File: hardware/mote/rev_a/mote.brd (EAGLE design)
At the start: 160 x 100 mm, 13 parts, among them U1 NRF52840

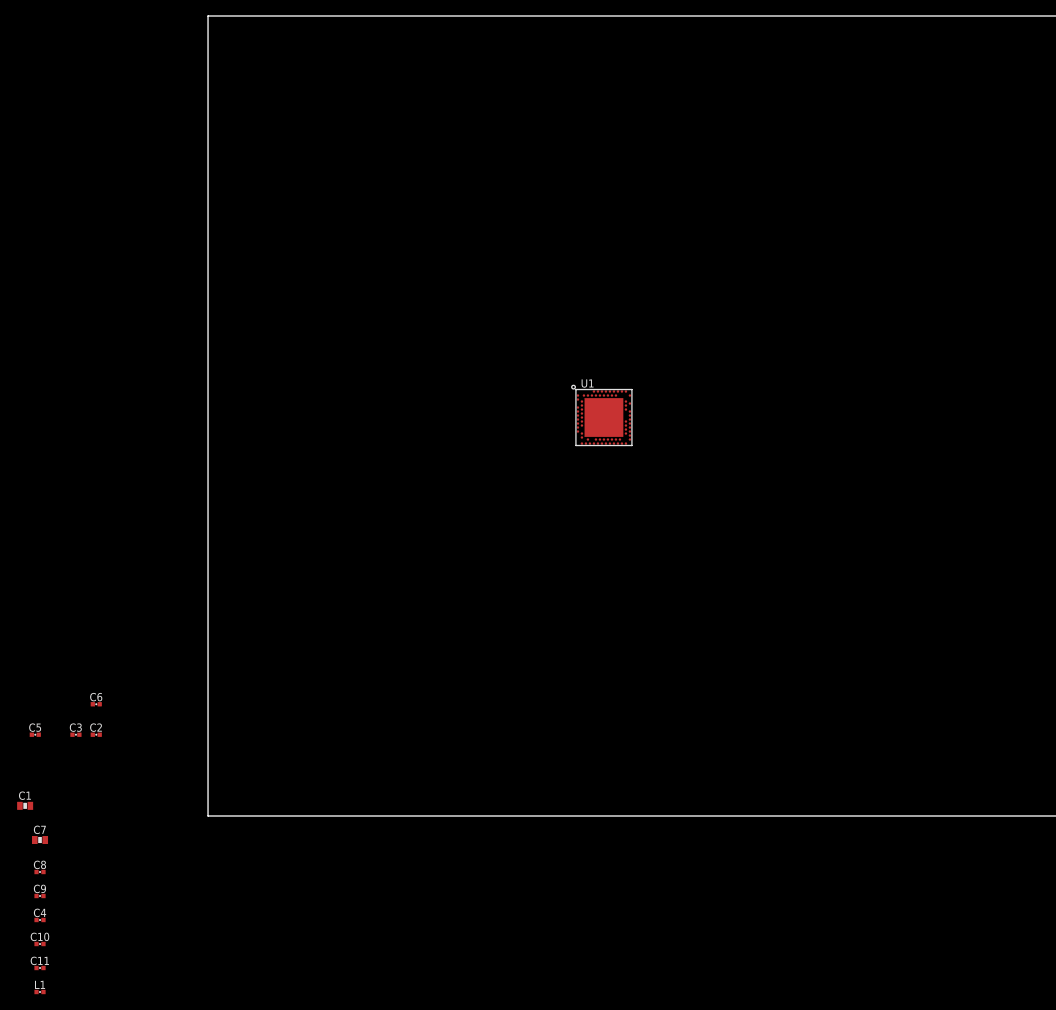
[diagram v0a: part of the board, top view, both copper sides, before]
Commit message: NRF + passives schematic done
Placement on board and preliminary routing
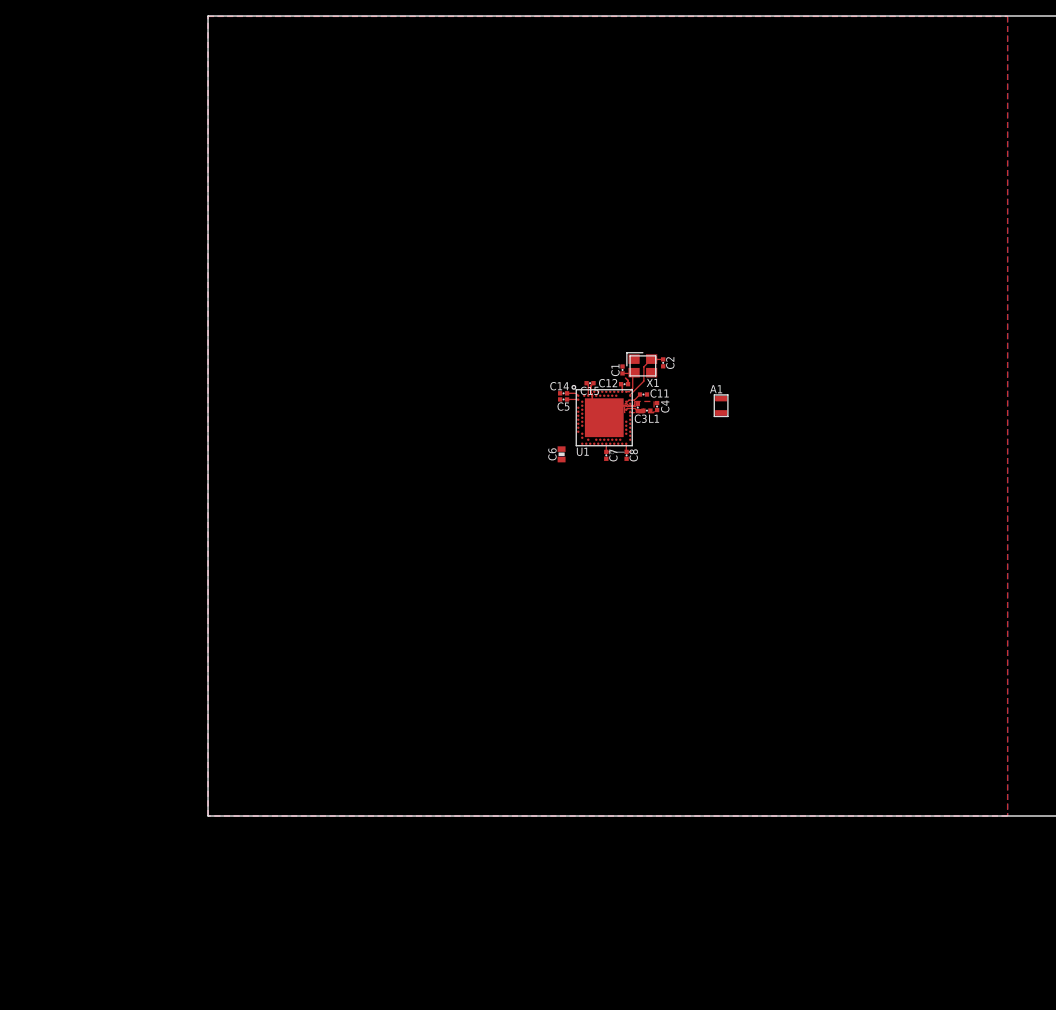
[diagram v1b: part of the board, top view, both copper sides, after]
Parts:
- removed C10: 0.8pF, passives:0402_CAP
- removed C9: 12pF, passives:0402_CAP
- added A1: (no value), chips:AH212M
- added C12: 100nF, passives:0402_CAP
- added C14, C15: 1.0uF, passives:0402_CAP
- added X1: 7V-32.000MAHV-T, crystals:TXC-7V
- C1: value 4.7uF -> 12pF; device passives:0603_CAP -> passives:0402_CAP
- C11: value 0.5pF -> 100pF
- C2: value 100nF -> 12pF
- C3: value 100nF -> 0.8pF
- C4: value 12pF -> 0.5pF
- C6: value 100nF -> 4.7uF; device passives:0402_CAP -> passives:0603_CAP
- C7: value 1.0uF -> 100nF; device passives:0603_CAP -> passives:0402_CAP
- C8: value 100pF -> 100nF
- moved L1 105.1 mm to (54.9, 50.7), turned to 180 degrees
- moved C11 104.1 mm to (54.4, 52.7)
- moved C4 100.3 mm to (56.1, 51.2), turned to 90 degrees
- moved C1 92.4 mm to (51.8, 55.8), turned to 270 degrees
- moved C8 89.9 mm to (52.3, 45.1), turned to 270 degrees
- moved C7 85.6 mm to (49.8, 45.1), turned to 270 degrees
- moved C2 84.8 mm to (56.9, 56.6), turned to 90 degrees
- moved C3 81.3 mm to (53.7, 51.1), turned to 90 degrees
- moved C5 78.2 mm to (44.5, 52.1), turned to 180 degrees
- moved C6 66.0 mm to (44.2, 45.2), turned to 270 degrees
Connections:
- new net GND: C1.1, C11.2, C12.2, C14.2, C15.2, C2.1, C3.2, C4.2, C5.2, C6.2, C7.2, C8.2, U1.AD2, U1.B7, U1.F23, U1.GND, X1.2, X1.4
- new net N$1: C12.1, C14.1, C6.1, C7.1, C8.1, U1.A22, U1.AD14, U1.AD23, U1.B1, U1.W1, U1.Y2
- new net N$2: C5.1, U1.C1
- new net N$3: C15.1, U1.B5
- new net N$4: C11.1, U1.D23
- new net N$5: C3.1, L1.2, U1.H23
- new net N$6: A1.P1, C4.1, L1.1
- new net N$8: C2.2, U1.B24, X1.3
- new net N$9: C1.2, U1.A23, X1.1
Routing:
- net GND: track 0.00 -> 11.1 mm
- net N$1: track 0.00 -> 8.68 mm, vias 0 -> 2
- net N$8: track 0.00 -> 7.15 mm
- net N$9: track 0.00 -> 4.42 mm
- net N$5: track 0.00 -> 2.39 mm
- net N$4: track 0.00 -> 2.10 mm
- net N$3: track 0.00 -> 1.66 mm
- net N$2: track 0.00 -> 1.41 mm
- added copper zone on layer 1, net GND
- added copper zone on layer 16, net GND
- added copper zone on layer 1, net N$7

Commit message: front end overvolt
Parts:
- added BAT1: LTOHTC1020, batteries:1020
- added C13, C16: 10uF, passives:0603_CAP
- added D1: SOLARCELL, mote:SOLAR_HOLES
- added L3: 1uH, passives:IHL-2525CZ
- added Q1: CSD22206W, fets:CSD22206W
- added R1: 1k, passives:0402_RES
- added R2: 80.6k, passives:0603-RES
- added R3: 20, passives:0402_RES
- added R4: 33M, passives:0603-RES
- added U2: (no value), chips:WLCSP-6
- added U3: MAX17222, chips:UDFN-6-MAXIM
- added U4: TPS3839G25DBZ, chips:SOT-23
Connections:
- new net ENABLE: R4.2
- new net N$10: BAT1.-, D1.-, R3.1, U2.A2, U2.B2
- new net N$11: Q1.A1, R1.1, U2.C2
- new net N$12: R2.2, U3.4
- new net N$13: Q1.A2, Q1.A3, Q1.B1, Q1.B2, Q1.B3, R3.2, U4.1
- new net N$14: R4.1, U3.6
- new net SW1: L3.P$2, U3.2
- new net VBAT: C13.1, L3.P$1, U3.5
- new net VCC: C12.1, C14.1, C16.1, C6.1, C7.1, C8.1, U1.A22, U1.AD14, U1.AD23, U1.B1, U1.W1, U1.Y2, U3.1
- net GND: now also C13.2, C16.2, R2.1, U3.3
- net N$1: now also BAT1.+, D1.+, Q1.C1, Q1.C2, Q1.C3, R1.2, U2.A1, U2.C1, U4.3; no longer C12.1, C14.1, C6.1, C7.1, C8.1, U1.A22, U1.AD14, U1.AD23, U1.B1, U1.W1, U1.Y2
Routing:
- net SW1: track 0.00 -> 19.2 mm
- net VBATT: track 0.00 -> 15.9 mm
- net VOUT1: track 0.00 -> 13.2 mm
- net N$1: track 8.68 -> 0.00 mm, vias 2 -> 0
- net N$14: track 0.00 -> 7.28 mm
- net VCC: track 0.00 -> 6.14 mm, vias 0 -> 2
- net VBAT: track 0.00 -> 4.63 mm
- net N$12: track 0.00 -> 3.81 mm
- net ENABLE: track 0.00 -> 3.16 mm
- net GND: vias 0 -> 3
- added copper zone on layer 1, net SW1
- added copper zone on layer 1, net VBATT
- added copper zone on layer 1, net VOUT1
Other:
- board text added: "DISABLE"
- board text added: "ENABLE"

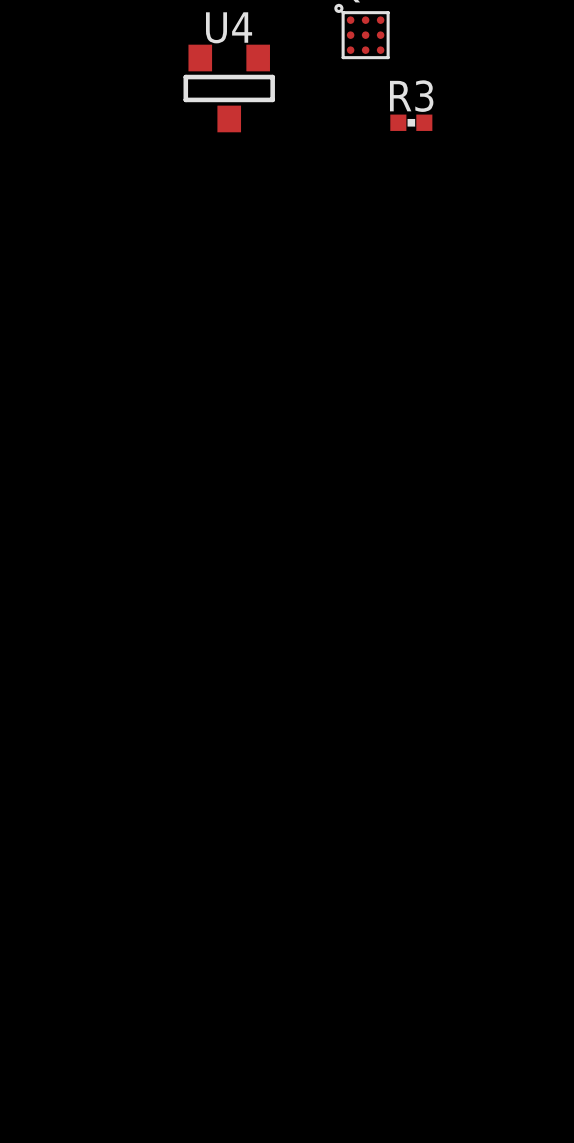
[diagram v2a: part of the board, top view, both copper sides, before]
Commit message: Add start of source switching
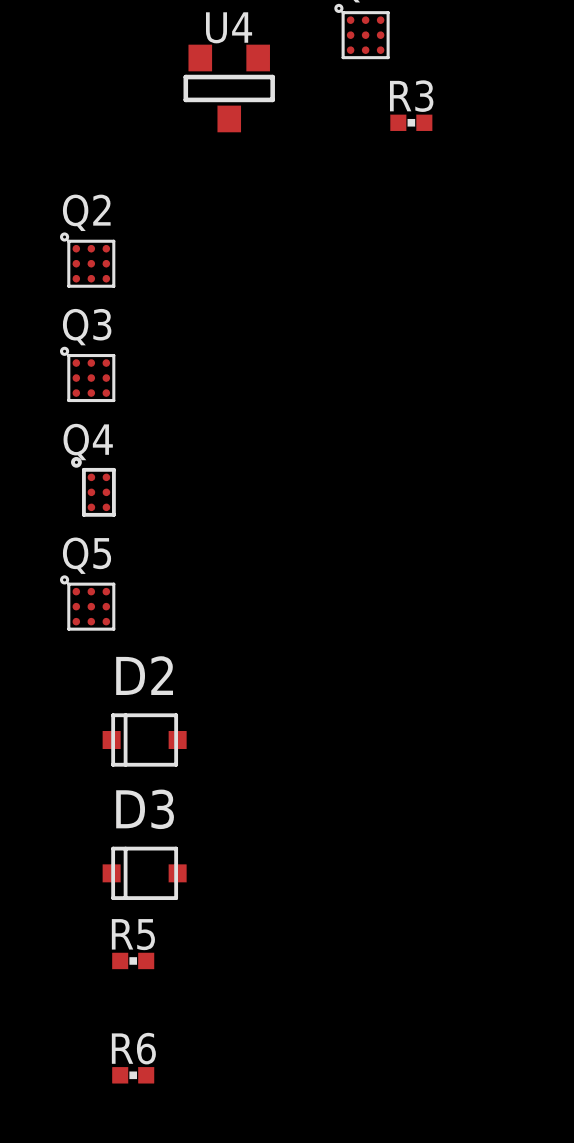
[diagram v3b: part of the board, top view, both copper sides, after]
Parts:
- added D2, D3: DIODE_SCHOTTKYSOD323, passives:SOD323
- added Q2, Q3: CSD75207W15, fets:DSBGA
- added Q4: CSD13303W1015, fets:6DSBGA
- added Q5: CSD22206W, fets:DSBGA
- added R5, R6: 100k, passives:0402_RES
- Q1: device fets:CSD22206W -> fets:DSBGA
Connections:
- new net N$15: D3.P$2, Q4.A1, Q4.B1, Q4.C1, Q5.A2, Q5.A3, Q5.B1, Q5.B2, Q5.B3, R6.1
- new net N$16: D3.P$1, R6.2
- new net N$17: Q1.A2, Q1.A3, Q1.B1, Q1.B2, Q1.B3, R3.2
- net GND: now also BAT1.-, D1.-, Q4.B2, Q4.C2, R3.1, U2.A2, U2.B2, U4.1
- net N$1: now also Q5.C1, Q5.C2, Q5.C3
- net N$10: now also D2.P$2, Q4.A2, Q5.A1, R5.1, U4.2; no longer BAT1.-, D1.-, R3.1, U2.A2, U2.B2
- net N$13: now also D2.P$1, R5.2; no longer Q1.A2, Q1.A3, Q1.B1, Q1.B2, Q1.B3, R3.2, U4.1
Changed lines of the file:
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@@
 </element>
 <element name="R1" library="passives" package="0402_RES" value="1k" x="0.762" y="-32.893"/>
-<element name="Q1" library="fets" package="CSD22206W" value="CSD22206W" x="-0.762" y="-37.592">
-<attribute name="DIGIKEY" value="296-47005-1-ND" x="-0.762" y="-37.592" size="1.778" layer="27" display="off"/>
+<element name="Q1" library="fets" package="DSBGA" value="CSD22206W" x="-0.762" y="-37.592">
+<attribute name="DIGIKEY" value="296-47005-1-ND " x="-0.762" y="-37.592" size="1.778" layer="27" display="off"/>
 <attribute name="MANUFACTURER" value="TEXAS INSTRUMENTS" x="-0.762" y="-37.592" size="1.778" layer="27" display="off"/>
 <attribute name="MPN" value="CSD22206WT" x="-0.762" y="-37.592" size="1.778" layer="27" display="off"/>
@@
 <attribute name="MPN" value="TPS3839G25DBZR" x="-5.334" y="-39.37" size="1.778" layer="27" display="off"/>
 </element>
+<element name="Q2" library="fets" package="DSBGA" value="CSD75207W15" x="-9.906" y="-45.212">
+<attribute name="DIGIKEY" value="296-40008-1-ND" x="-9.906" y="-45.212" size="1.778" layer="27" display="off"/>
+<attribute name="MANUFACTURER" value="TEXAS INSTRUMENTS" x="-9.906" y="-45.212" size="1.778" layer="27" display="off"/>
+<attribute name="MPN" value="CSD75207W15" x="-9.906" y="-45.212" size="1.778" layer="27" display="off"/>
+</element>
+<element name="Q3" library="fets" package="DSBGA" value="CSD75207W15" x="-9.906" y="-49.022">
+<attribute name="DIGIKEY" value="296-40008-1-ND" x="-9.906" y="-49.022" size="1.778" layer="27" display="off"/>
+<attribute name="MANUFACTURER" value="TEXAS INSTRUMENTS" x="-9.906" y="-49.022" size="1.778" layer="27" display="off"/>
+<attribute name="MPN" value="CSD75207W15" x="-9.906" y="-49.022" size="1.778" layer="27" display="off"/>
+</element>
+<element name="Q4" library="fets" package="6DSBGA" value="CSD13303W1015" x="-9.652" y="-52.832">
+<attribute name="DIGIKEY" value="296-39990-1-ND" x="-9.652" y="-52.832" size="1.778" layer="27" display="off"/>
+<attribute name="MANUFACTURER" value="TEXAS INSTRUMENTS" x="-9.652" y="-52.832" size="1.778" layer="27" display="off"/>
+<attribute name="MPN" value="CSD13303W1015" x="-9.652" y="-52.832" size="1.778" layer="27" display="off"/>
+</element>
+<element name="Q5" library="fets" package="DSBGA" value="CSD22206W" x="-9.906" y="-56.642">
+<attribute name="DIGIKEY" value="296-47005-1-ND " x="-9.906" y="-56.642" size="1.778" layer="27" display="off"/>
+<attribute name="MANUFACTURER" value="TEXAS INSTRUMENTS" x="-9.906" y="-56.642" size="1.778" layer="27" display="off"/>
+<attribute name="MPN" value="CSD22206WT" x="-9.906" y="-56.642" size="1.778" layer="27" display="off"/>
+</element>
+<element name="D2" library="passives" package="SOD323" value="DIODE_SCHOTTKYSOD323" x="-8.128" y="-61.087"/>
+<element name="D3" library="passives" package="SOD323" value="DIODE_SCHOTTKYSOD323" x="-8.128" y="-65.532"/>
+<element name="R5" library="passives" package="0402_RES" value="100k" x="-8.509" y="-68.453"/>
+<element name="R6" library="passives" package="0402_RES" value="100k" x="-8.509" y="-72.263"/>
 </elements>
 <signals>
@@
 <via x="33.147" y="21.717" extent="1-16" drill="0.762"/>
 <via x="26.797" y="15.621" extent="1-16" drill="0.762"/>
+<contactref element="U4" pad="1"/>
+<contactref element="Q4" pad="C2"/>
+<contactref element="Q4" pad="B2"/>
+<contactref element="R3" pad="1"/>
+<contactref element="D1" pad="-"/>
+<contactref element="BAT1" pad="-"/>
+<contactref element="U2" pad="B2"/>
+<contactref element="U2" pad="A2"/>
 <wire x1="55.456" y1="55.411" x2="56.896" y2="56.20893125" width="0" layer="19" extent="1-1"/>
 <wire x1="53.256" y1="57.111" x2="55.456" y2="55.411" width="0" layer="19" extent="1-1"/>
@@
 <wire x1="29.083" y1="15.987" x2="32.258" y2="15.987" width="0" layer="19" extent="1-1"/>
 <wire x1="26.797" y1="15.621" x2="29.083" y2="15.987" width="0" layer="19" extent="1-1"/>
+<wire x1="12.406" y1="-7.747" x2="26.797" y2="15.621" width="0" layer="19" extent="1-1"/>
+<wire x1="15.43" y1="-22.86" x2="12.406" y2="-7.747" width="0" layer="19" extent="1-1"/>
+<wire x1="-0.77" y1="-28.972" x2="15.43" y2="-22.86" width="0" layer="19" extent="1-1"/>
+<wire x1="-0.77" y1="-29.472" x2="-0.77" y2="-28.972" width="0" layer="19" extent="1-1"/>
+<wire x1="-4.3434" y1="-38.354" x2="-0.77" y2="-29.472" width="0" layer="19" extent="1-1"/>
+<wire x1="0.32893125" y1="-40.513" x2="-4.3434" y2="-38.354" width="0" layer="19" extent="1-1"/>
+<wire x1="-9.402" y1="-52.832" x2="-4.3434" y2="-38.354" width="0" layer="19" extent="1-1"/>
+<wire x1="-9.402" y1="-53.332" x2="-9.402" y2="-52.832" width="0" layer="19" extent="1-1"/>
 </signal>
 <signal name="N$8">
@@
 <contactref element="Q1" pad="C3"/>
 <contactref element="U4" pad="3"/>
+<contactref element="Q5" pad="C1"/>
+<contactref element="Q5" pad="C3"/>
+<contactref element="Q5" pad="C2"/>
+<wire x1="-9.906" y1="-57.142" x2="-10.406" y2="-57.142" width="0" layer="19" extent="1-1"/>
+<wire x1="-9.406" y1="-57.142" x2="-9.906" y2="-57.142" width="0" layer="19" extent="1-1"/>
+<wire x1="-5.3086" y1="-40.386" x2="-9.406" y2="-57.142" width="0" layer="19" extent="1-1"/>
 <wire x1="-1.262" y1="-38.092" x2="-5.3086" y2="-40.386" width="0" layer="19" extent="1-1"/>
 <wire x1="-0.762" y1="-38.092" x2="-1.262" y2="-38.092" width="0" layer="19" extent="1-1"/>
@@
 <wire x1="7.406" y1="-7.747" x2="7.43" y2="-22.86" width="0" layer="19" extent="1-1"/>
 </signal>
-<signal name="N$10">
-<contactref element="D1" pad="-"/>
-<contactref element="BAT1" pad="-"/>
-<contactref element="U2" pad="B2"/>
-<contactref element="U2" pad="A2"/>
-<contactref element="R3" pad="1"/>
-<wire x1="-0.77" y1="-29.472" x2="0.32893125" y2="-40.513" width="0" layer="19" extent="1-1"/>
-<wire x1="-0.77" y1="-28.972" x2="-0.77" y2="-29.472" width="0" layer="19" extent="1-1"/>
-<wire x1="15.43" y1="-22.86" x2="-0.77" y2="-28.972" width="0" layer="19" extent="1-1"/>
-<wire x1="12.406" y1="-7.747" x2="15.43" y2="-22.86" width="0" layer="19" extent="1-1"/>
-</signal>
 <signal name="N$11">
 <contactref element="U2" pad="C2"/>
@@
 <wire x1="-0.77" y1="-29.972" x2="0.32893125" y2="-32.893" width="0" layer="19" extent="1-1"/>
 </signal>
-<signal name="N$13">
+<signal name="N$15">
+<contactref element="Q5" pad="B1"/>
+<contactref element="Q5" pad="A2"/>
+<contactref element="Q5" pad="B2"/>
+<contactref element="Q5" pad="A3"/>
+<contactref element="Q5" pad="B3"/>
+<contactref element="Q4" pad="B1"/>
+<contactref element="Q4" pad="C1"/>
+<contactref element="Q4" pad="A1"/>
+<contactref element="D3" pad="P$2"/>
+<contactref element="R6" pad="1"/>
+<wire x1="-7.028" y1="-65.532" x2="-8.94206875" y2="-72.263" width="0" layer="19" extent="1-1"/>
+<wire x1="-9.406" y1="-56.642" x2="-7.028" y2="-65.532" width="0" layer="19" extent="1-1"/>
+<wire x1="-9.906" y1="-56.642" x2="-9.406" y2="-56.642" width="0" layer="19" extent="1-1"/>
+<wire x1="-10.406" y1="-56.642" x2="-9.906" y2="-56.642" width="0" layer="19" extent="1-1"/>
+<wire x1="-9.906" y1="-56.142" x2="-9.906" y2="-56.642" width="0" layer="19" extent="1-1"/>
+<wire x1="-9.406" y1="-56.142" x2="-9.406" y2="-56.642" width="0" layer="19" extent="1-1"/>
+<wire x1="-9.902" y1="-53.332" x2="-9.906" y2="-56.142" width="0" layer="19" extent="1-1"/>
+<wire x1="-9.902" y1="-52.832" x2="-9.902" y2="-53.332" width="0" layer="19" extent="1-1"/>
+<wire x1="-9.902" y1="-52.332" x2="-9.902" y2="-52.832" width="0" layer="19" extent="1-1"/>
+</signal>
+<signal name="N$17">
 <contactref element="R3" pad="2"/>
 <contactref element="Q1" pad="B1"/>
 <contactref element="Q1" pad="A2"/>
+<contactref element="Q1" pad="B2"/>
 <contactref element="Q1" pad="A3"/>
 <contactref element="Q1" pad="B3"/>
-<contactref element="Q1" pad="B2"/>
-<contactref element="U4" pad="1"/>
-<wire x1="-1.262" y1="-37.592" x2="-4.3434" y2="-38.354" width="0" layer="19" extent="1-1"/>
-<wire x1="-0.762" y1="-37.592" x2="-1.262" y2="-37.592" width="0" layer="19" extent="1-1"/>
+<wire x1="-0.262" y1="-37.592" x2="1.19506875" y2="-40.513" width="0" layer="19" extent="1-1"/>
+<wire x1="-0.762" y1="-37.592" x2="-0.262" y2="-37.592" width="0" layer="19" extent="1-1"/>
+<wire x1="-1.262" y1="-37.592" x2="-0.762" y2="-37.592" width="0" layer="19" extent="1-1"/>
 <wire x1="-0.762" y1="-37.092" x2="-0.762" y2="-37.592" width="0" layer="19" extent="1-1"/>
-<wire x1="-0.262" y1="-37.092" x2="-0.762" y2="-37.092" width="0" layer="19" extent="1-1"/>
-<wire x1="-0.262" y1="-37.592" x2="-0.762" y2="-37.592" width="0" layer="19" extent="1-1"/>
-<wire x1="1.19506875" y1="-40.513" x2="-0.262" y2="-37.592" width="0" layer="19" extent="1-1"/>
+<wire x1="-0.262" y1="-37.092" x2="-0.262" y2="-37.592" width="0" layer="19" extent="1-1"/>
+</signal>
+<signal name="N$10">
+<contactref element="D2" pad="P$2"/>
+<contactref element="R5" pad="1"/>
+<contactref element="U4" pad="2"/>
+<contactref element="Q5" pad="A1"/>
+<contactref element="Q4" pad="A2"/>
+<wire x1="-7.028" y1="-61.087" x2="-8.94206875" y2="-68.453" width="0" layer="19" extent="1-1"/>
+<wire x1="-10.406" y1="-56.142" x2="-7.028" y2="-61.087" width="0" layer="19" extent="1-1"/>
+<wire x1="-9.402" y1="-52.332" x2="-10.406" y2="-56.142" width="0" layer="19" extent="1-1"/>
+<wire x1="-6.2738" y1="-38.354" x2="-9.402" y2="-52.332" width="0" layer="19" extent="1-1"/>
+</signal>
+<signal name="N$13">
+<contactref element="D2" pad="P$1"/>
+<contactref element="R5" pad="2"/>
+<wire x1="-9.228" y1="-61.087" x2="-8.07593125" y2="-68.453" width="0" layer="19" extent="1-1"/>
+</signal>
+<signal name="N$16">
+<contactref element="D3" pad="P$1"/>
+<contactref element="R6" pad="2"/>
+<wire x1="-9.228" y1="-65.532" x2="-8.07593125" y2="-72.263" width="0" layer="19" extent="1-1"/>
 </signal>
 </signals>
